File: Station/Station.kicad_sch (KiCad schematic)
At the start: 3 parts, among them U1 ATmega328P-A, U2 CH340N

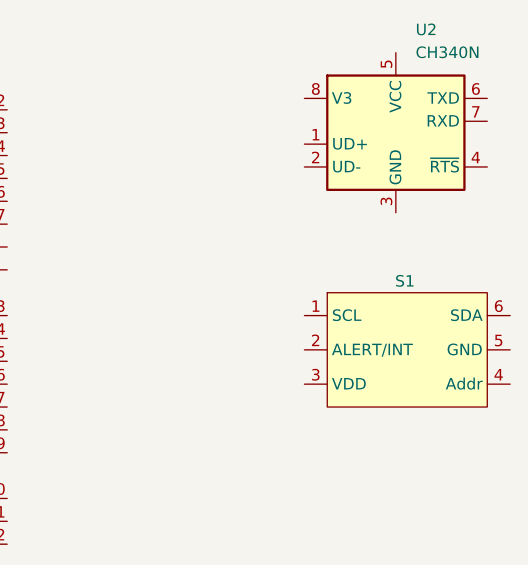
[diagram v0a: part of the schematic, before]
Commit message: Added switch footprint and symbol
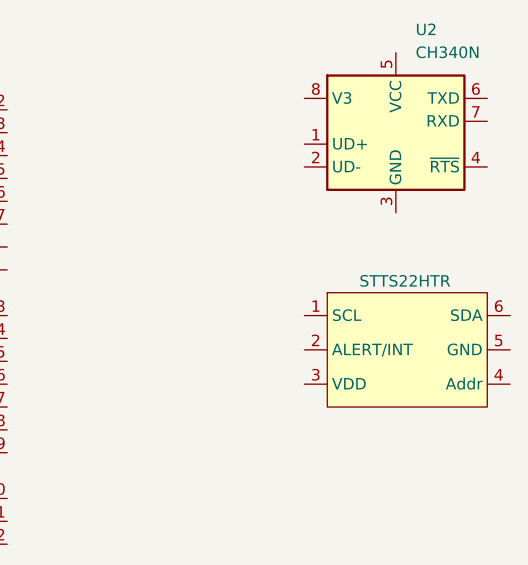
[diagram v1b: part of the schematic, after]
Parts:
- renumbered S1 to STTS22HTR
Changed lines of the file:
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@@
 		(on_board yes)
 		(dnp no)
-		(property "Reference" "S1"
+		(property "Reference" "STTS22HTR"
 			(at 101.346 46.99 0)
 			(effects
@@
 			(project ""
 				(path "/7f7e2b09-5167-49f8-a89c-b41fa1731313"
-					(reference "S1")
+					(reference "STTS22HTR")
 					(unit 1)
 				)

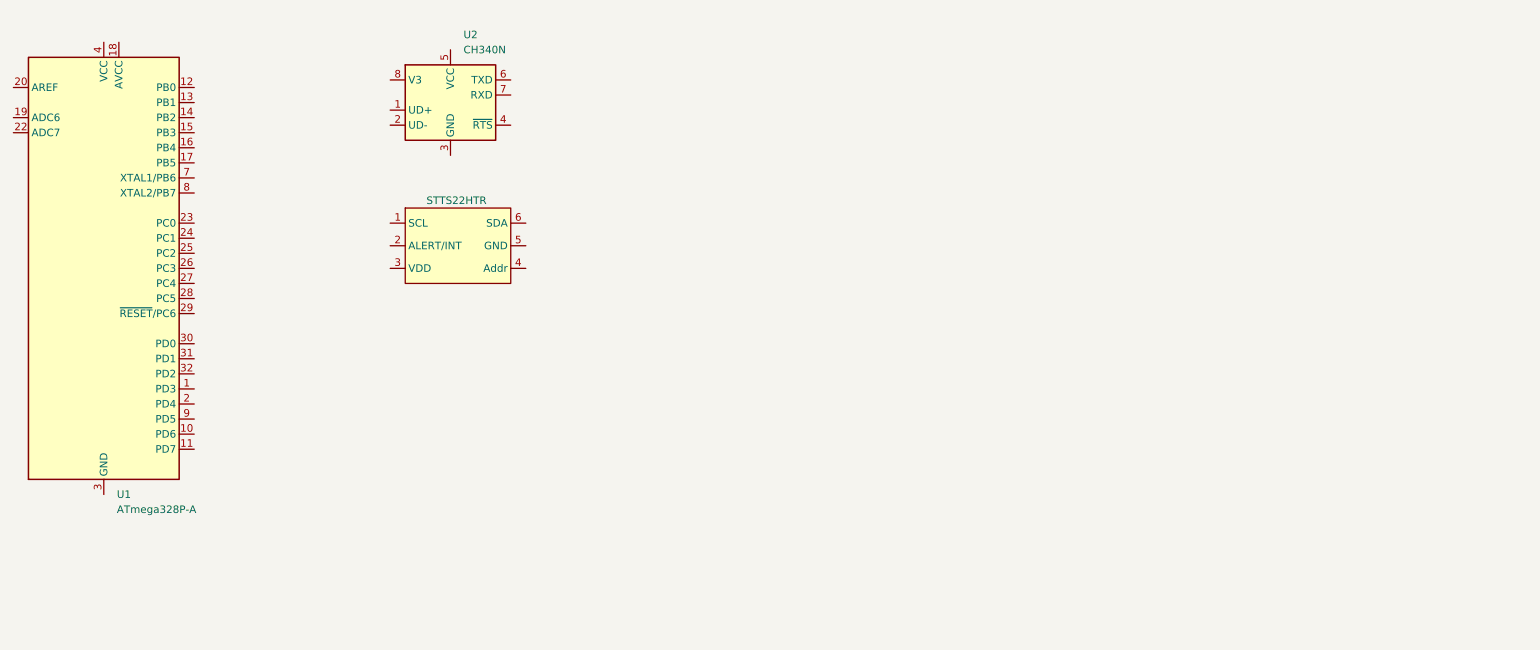
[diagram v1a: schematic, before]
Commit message: Switch footprint, MCU schematics
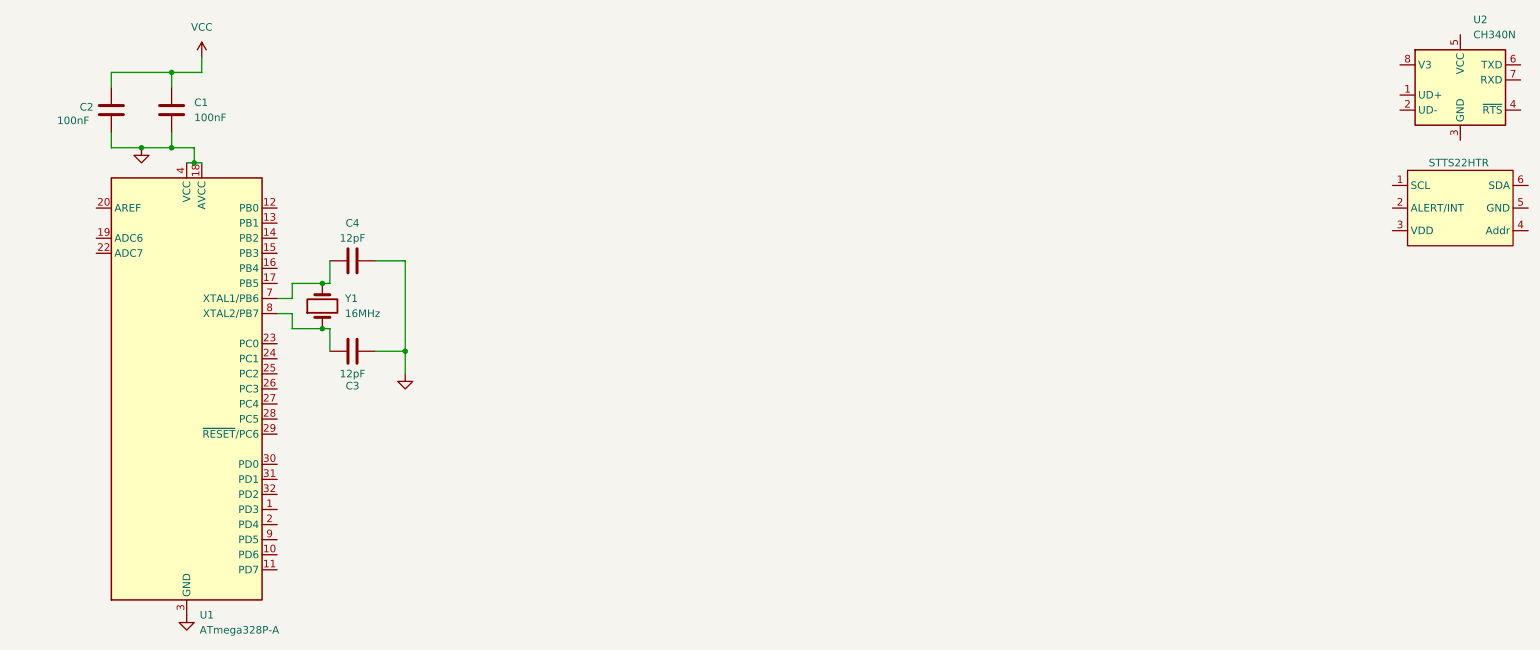
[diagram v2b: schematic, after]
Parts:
- added C1, C2: 100nF, symbol Device:C
- added C3, C4: 12pF, symbol Device:C
- added Y1: 16MHz, symbol Device:Crystal
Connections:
- net GND: now reaches U1.18 (AVCC)
- net GND: now also U1.21 (GND), U1.3 (GND), U1.4 (VCC), U1.5 (GND), U1.6 (VCC), C1.2, C2.2, C3.2, C4.2
- net at U1.7 (XTAL1/PB6): now also C4.1, Y1.2
- net at U1.8 (XTAL2/PB7): now also C3.1, Y1.1
- new net VCC: C1.1, C2.1
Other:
- moved on the sheet: STTS22HTR, U1, U2
